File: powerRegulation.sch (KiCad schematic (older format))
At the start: 6 parts

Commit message: added additional regulator to power the ACS711 and potentially a micro at 3.3V
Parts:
- added C?: 4.7uF, symbol C
- added C?: 10uF, symbol C
- added L?: 4.7uH, symbol INDUCTOR_SMALL
- added R?: 976K, symbol R
- added R?: 562K, symbol R
- added U?: MCP1640T, SOT-23-6, symbol MCP1640T
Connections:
- net labels added: 3.3V
- wire segments 20 -> 45
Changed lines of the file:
@@
 Connection ~ 7200 2750
 Wire Wire Line
-	7200 3200 7200 2750
+	7200 2750 7200 3200
 Connection ~ 6800 2750
 Wire Wire Line
@@
 Connection ~ 6800 3950
 Wire Wire Line
-	7200 3600 7200 3950
+	7200 3950 7200 3600
 Connection ~ 5200 3950
 Wire Wire Line
@@
 	5800 3950 5800 4100
 Wire Wire Line
-	7200 3950 4850 3950
+	4850 3950 7200 3950
 Connection ~ 6800 3400
 Wire Wire Line
@@
 	6250 2900 6550 2900
 Wire Wire Line
-	6800 3450 6800 3350
+	6800 3350 6800 3450
 Text GLabel 8050 2750 2    60   Output ~ 0
 2.7V
@@
 Wire Wire Line
 	3900 2750 5350 2750
+$Comp
+L MCP1640T U?
+U 1 1 5522881E
+P 6550 4900
+F 0 "U?" H 6800 4650 40  0000 C CNN
+F 1 "MCP1640T" H 6800 5200 40  0000 C CNN
+F 2 "SOT-23-6" H 6550 4950 30  0000 C CIN
+F 3 "" H 6550 4900 60  0000 C CNN
+	1    6550 4900
+	1    0    0    -1
+$EndComp
+$Comp
+L INDUCTOR_SMALL L?
+U 1 1 55228894
+P 6000 4500
+F 0 "L?" H 6000 4600 50  0000 C CNN
+F 1 "4.7uH" H 6000 4450 50  0000 C CNN
+F 2 "" H 6000 4500 60  0000 C CNN
+F 3 "" H 6000 4500 60  0000 C CNN
+F 4 "Value" H 6000 4500 60  0001 C CNN "MPN"
+	1    6000 4500
+	1    0    0    -1
+$EndComp
+Wire Wire Line
+	6250 4500 6550 4500
+$Comp
+L GND #PWR?
+U 1 1 55228946
+P 6550 5450
+F 0 "#PWR?" H 6550 5200 60  0001 C CNN
+F 1 "GND" H 6550 5300 60  0000 C CNN
+F 2 "" H 6550 5450 60  0000 C CNN
+F 3 "" H 6550 5450 60  0000 C CNN
+	1    6550 5450
+	1    0    0    -1
+$EndComp
+Wire Wire Line
+	6550 5200 6550 5450
+Text GLabel 5250 4750 0    60   Input ~ 0
+2.7V
+Wire Wire Line
+	5250 4750 6100 4750
+Wire Wire Line
+	6100 4900 5950 4900
+Wire Wire Line
+	5950 4900 5950 4750
+Connection ~ 5950 4750
+$Comp
+L C C?
+U 1 1 55228B01
+P 5750 5150
+F 0 "C?" H 5800 5250 50  0000 L CNN
+F 1 "4.7uF" H 5800 5050 50  0000 L CNN
+F 2 "" H 5788 5000 30  0000 C CNN
+F 3 "" H 5750 5150 60  0000 C CNN
+F 4 "Value" H 5750 5150 60  0001 C CNN "MPN"
+	1    5750 5150
+	1    0    0    -1
+$EndComp
+Wire Wire Line
+	5750 4950 5750 4750
+Connection ~ 5750 4750
+Wire Wire Line
+	5750 5350 5750 5400
+Wire Wire Line
+	5750 5400 6550 5400
+Connection ~ 6550 5400
+Wire Wire Line
+	5750 4500 5550 4500
+Wire Wire Line
+	5550 4500 5550 4750
+Connection ~ 5550 4750
+$Comp
+L R R?
+U 1 1 55228C70
+P 7700 5050
+F 0 "R?" V 7780 5050 50  0000 C CNN
+F 1 "976K" V 7707 5051 50  0000 C CNN
+F 2 "" V 7630 5050 30  0000 C CNN
+F 3 "" H 7700 5050 30  0000 C CNN
+	1    7700 5050
+	1    0    0    -1
+$EndComp
+$Comp
+L R R?
+U 1 1 55228CAB
+P 7700 5650
+F 0 "R?" V 7780 5650 50  0000 C CNN
+F 1 "562K" V 7707 5651 50  0000 C CNN
+F 2 "" V 7630 5650 30  0000 C CNN
+F 3 "" H 7700 5650 30  0000 C CNN
+	1    7700 5650
+	1    0    0    -1
+$EndComp
+Text GLabel 8100 4750 2    60   Input ~ 0
+3.3V
+Wire Wire Line
+	7000 4750 8100 4750
+Wire Wire Line
+	7700 4800 7700 4750
+Connection ~ 7700 4750
+Wire Wire Line
+	7700 5300 7700 5400
+Wire Wire Line
+	7000 4900 7400 4900
+Wire Wire Line
+	7400 4900 7400 5350
+Wire Wire Line
+	7400 5350 7700 5350
+Connection ~ 7700 5350
+Wire Wire Line
+	7700 5900 7700 6000
+Wire Wire Line
+	7700 6000 7050 6000
+Wire Wire Line
+	7050 6000 7050 5300
+Wire Wire Line
+	7050 5300 6550 5300
+Connection ~ 6550 5300
+$Comp
+L C C?
+U 1 1 5522902B
+P 7950 5300
+F 0 "C?" H 8000 5400 50  0000 L CNN
+F 1 "10uF" H 8000 5200 50  0000 L CNN
+F 2 "" H 7988 5150 30  0000 C CNN
+F 3 "" H 7950 5300 60  0000 C CNN
+	1    7950 5300
+	1    0    0    -1
+$EndComp
+Wire Wire Line
+	7950 5100 7950 4750
+Connection ~ 7950 4750
+Wire Wire Line
+	7950 5500 7950 6050
+Wire Wire Line
+	7950 6050 6900 6050
+Wire Wire Line
+	6900 6050 6900 5350
+Wire Wire Line
+	6900 5350 6550 5350
+Connection ~ 6550 5350
 $EndSCHEMATC

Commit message: updated power regulation circuit with a different component so that the pin numbers now show
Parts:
- removed U?: LM2931D-R, symbol LM2931D-R
- added U?: LM2931, SO-8, symbol LM2931
- C?: value C -> 0.1uF
- C?: value C -> 100uF
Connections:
- wire segments 45 -> 65
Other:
- moved on the sheet: C?
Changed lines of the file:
@@
 L C C?
 U 1 1 5521C44E
-P 4850 3650
-F 0 "C?" H 4900 3750 50  0000 L CNN
-F 1 "C" H 4900 3550 50  0000 L CNN
-F 2 "" H 4888 3500 30  0000 C CNN
-F 3 "" H 4850 3650 60  0000 C CNN
-	1    4850 3650
+P 4850 3300
+F 0 "C?" H 4900 3400 50  0000 L CNN
+F 1 "0.1uF" H 4900 3200 50  0000 L CNN
+F 2 "" H 4888 3150 30  0000 C CNN
+F 3 "" H 4850 3300 60  0000 C CNN
+	1    4850 3300
 	-1   0    0    -1
 $EndComp
@@
 L C C?
 U 1 1 5521C455
-P 7200 3400
-F 0 "C?" H 7250 3500 50  0000 L CNN
-F 1 "C" H 7250 3300 50  0000 L CNN
-F 2 "" H 7238 3250 30  0000 C CNN
-F 3 "" H 7200 3400 60  0000 C CNN
-	1    7200 3400
-	-1   0    0    -1
-$EndComp
-$Comp
-L LM2931D-R U?
-U 1 1 5521C45C
-P 5800 3150
-F 0 "U?" H 6100 3100 60  0000 C CNN
-F 1 "LM2931D-R" H 5800 3650 60  0000 C CNN
-F 2 "" H 5650 3350 60  0000 C CNN
-F 3 "" H 5650 3350 60  0000 C CNN
-	1    5800 3150
-	1    0    0    -1
+P 7200 3300
+F 0 "C?" H 7250 3400 50  0000 L CNN
+F 1 "100uF" H 7250 3200 50  0000 L CNN
+F 2 "" H 7238 3150 30  0000 C CNN
+F 3 "" H 7200 3300 60  0000 C CNN
+	1    7200 3300
+	-1   0    0    -1
 $EndComp
 $Comp
@@
 	-1   0    0    -1
 $EndComp
-Connection ~ 7200 2750
-Wire Wire Line
-	7200 2750 7200 3200
-Connection ~ 6800 2750
-Wire Wire Line
-	6800 2850 6800 2750
-Connection ~ 6800 3950
-Wire Wire Line
-	7200 3950 7200 3600
-Connection ~ 5200 3950
-Wire Wire Line
-	5200 3550 5200 3950
-Wire Wire Line
-	5200 2900 5200 3050
-Wire Wire Line
-	5350 2900 5200 2900
-Connection ~ 4850 2750
-Wire Wire Line
-	4850 3450 4850 2750
-Connection ~ 5650 3950
-Wire Wire Line
-	4850 3950 4850 3850
-Connection ~ 5750 3950
-Wire Wire Line
-	5650 3950 5650 3200
-Connection ~ 5800 3950
-Wire Wire Line
-	5750 3950 5750 3200
-Connection ~ 5950 3950
-Wire Wire Line
-	5950 3200 5950 3950
-Connection ~ 5850 3950
-Wire Wire Line
-	5850 3200 5850 3950
-Wire Wire Line
-	5800 3950 5800 4100
-Wire Wire Line
-	4850 3950 7200 3950
-Connection ~ 6800 3400
-Wire Wire Line
-	6550 3400 6800 3400
-Wire Wire Line
-	6550 2900 6550 3400
-Wire Wire Line
-	6250 2900 6550 2900
-Wire Wire Line
-	6800 3350 6800 3450
 Text GLabel 8050 2750 2    60   Output ~ 0
 2.7V
-Wire Wire Line
-	6250 2750 8050 2750
 Text HLabel 3900 2750 0    60   Input ~ 0
 Vin
-Wire Wire Line
-	3900 2750 5350 2750
 $Comp
 L MCP1640T U?
@@
 	1    0    0    -1
 $EndComp
-Wire Wire Line
-	6250 4500 6550 4500
 $Comp
 L GND #PWR?
@@
 	1    0    0    -1
 $EndComp
-Wire Wire Line
-	6550 5200 6550 5450
 Text GLabel 5250 4750 0    60   Input ~ 0
 2.7V
-Wire Wire Line
-	5250 4750 6100 4750
-Wire Wire Line
-	6100 4900 5950 4900
-Wire Wire Line
-	5950 4900 5950 4750
-Connection ~ 5950 4750
 $Comp
 L C C?
@@
 	1    0    0    -1
 $EndComp
-Wire Wire Line
-	5750 4950 5750 4750
-Connection ~ 5750 4750
-Wire Wire Line
-	5750 5350 5750 5400
-Wire Wire Line
-	5750 5400 6550 5400
-Connection ~ 6550 5400
-Wire Wire Line
-	5750 4500 5550 4500
-Wire Wire Line
-	5550 4500 5550 4750
-Connection ~ 5550 4750
 $Comp
 L R R?
@@
 Text GLabel 8100 4750 2    60   Input ~ 0
 3.3V
-Wire Wire Line
-	7000 4750 8100 4750
-Wire Wire Line
-	7700 4800 7700 4750
-Connection ~ 7700 4750
-Wire Wire Line
-	7700 5300 7700 5400
-Wire Wire Line
-	7000 4900 7400 4900
-Wire Wire Line
-	7400 4900 7400 5350
-Wire Wire Line
-	7400 5350 7700 5350
-Connection ~ 7700 5350
-Wire Wire Line
-	7700 5900 7700 6000
-Wire Wire Line
-	7700 6000 7050 6000
-Wire Wire Line
-	7050 6000 7050 5300
-Wire Wire Line
-	7050 5300 6550 5300
-Connection ~ 6550 5300
 $Comp
 L C C?
@@
 	1    0    0    -1
 $EndComp
+Connection ~ 7200 2750
+Wire Wire Line
+	7200 2750 7200 3100
+Connection ~ 6800 2750
+Wire Wire Line
+	6800 2850 6800 2750
+Connection ~ 6800 3950
+Wire Wire Line
+	7200 3950 7200 3500
+Connection ~ 5200 3950
+Wire Wire Line
+	5200 3550 5200 3950
+Wire Wire Line
+	5200 2850 5200 3050
+Connection ~ 4850 2750
+Wire Wire Line
+	4850 3100 4850 2750
+Connection ~ 5650 3950
+Wire Wire Line
+	4850 3950 4850 3500
+Connection ~ 5750 3950
+Wire Wire Line
+	5650 3950 5650 3200
+Connection ~ 5800 3950
+Wire Wire Line
+	5750 3950 5750 3200
+Connection ~ 5950 3950
+Wire Wire Line
+	5950 3200 5950 3950
+Connection ~ 5850 3950
+Wire Wire Line
+	5850 3200 5850 3950
+Wire Wire Line
+	5800 3950 5800 4100
+Wire Wire Line
+	4850 3950 5200 3950
+Wire Wire Line
+	5200 3950 5650 3950
+Wire Wire Line
+	5650 3950 5750 3950
+Wire Wire Line
+	5750 3950 5800 3950
+Wire Wire Line
+	5800 3950 5850 3950
+Wire Wire Line
+	5850 3950 5950 3950
+Wire Wire Line
+	5950 3950 6800 3950
+Wire Wire Line
+	6800 3950 7200 3950
+Connection ~ 6800 3400
+Wire Wire Line
+	6550 3400 6800 3400
+Wire Wire Line
+	6550 2850 6550 3400
+Wire Wire Line
+	6800 3350 6800 3400
+Wire Wire Line
+	6800 3400 6800 3450
+Wire Wire Line
+	6200 2750 6800 2750
+Wire Wire Line
+	6800 2750 7200 2750
+Wire Wire Line
+	7200 2750 8050 2750
+Wire Wire Line
+	3900 2750 4850 2750
+Wire Wire Line
+	4850 2750 5400 2750
+Wire Wire Line
+	6250 4500 6550 4500
+Wire Wire Line
+	6550 5200 6550 5300
+Wire Wire Line
+	6550 5300 6550 5350
+Wire Wire Line
+	6550 5350 6550 5400
+Wire Wire Line
+	6550 5400 6550 5450
+Wire Wire Line
+	5250 4750 5550 4750
+Wire Wire Line
+	5550 4750 5750 4750
+Wire Wire Line
+	5750 4750 5950 4750
+Wire Wire Line
+	5950 4750 6100 4750
+Wire Wire Line
+	6100 4900 5950 4900
+Wire Wire Line
+	5950 4900 5950 4750
+Connection ~ 5950 4750
+Wire Wire Line
+	5750 4950 5750 4750
+Connection ~ 5750 4750
+Wire Wire Line
+	5750 5350 5750 5400
+Wire Wire Line
+	5750 5400 6550 5400
+Connection ~ 6550 5400
+Wire Wire Line
+	5750 4500 5550 4500
+Wire Wire Line
+	5550 4500 5550 4750
+Connection ~ 5550 4750
+Wire Wire Line
+	7000 4750 7700 4750
+Wire Wire Line
+	7700 4750 7950 4750
+Wire Wire Line
+	7950 4750 8100 4750
+Wire Wire Line
+	7700 4800 7700 4750
+Connection ~ 7700 4750
+Wire Wire Line
+	7700 5300 7700 5350
+Wire Wire Line
+	7700 5350 7700 5400
+Wire Wire Line
+	7000 4900 7400 4900
+Wire Wire Line
+	7400 4900 7400 5350
+Wire Wire Line
+	7400 5350 7700 5350
+Connection ~ 7700 5350
+Wire Wire Line
+	7700 5900 7700 6000
+Wire Wire Line
+	7700 6000 7050 6000
+Wire Wire Line
+	7050 6000 7050 5300
+Wire Wire Line
+	7050 5300 6550 5300
+Connection ~ 6550 5300
 Wire Wire Line
 	7950 5100 7950 4750
@@
 	6900 5350 6550 5350
 Connection ~ 6550 5350
+$Comp
+L LM2931 U?
+U 1 1 55220147
+P 5800 2800
+F 0 "U?" H 5600 3000 40  0000 C CNN
+F 1 "LM2931" H 5800 3000 40  0000 L CNN
+F 2 "SO-8" H 5800 2900 30  0000 C CIN
+F 3 "" H 5800 2700 60  0000 C CNN
+	1    5800 2800
+	1    0    0    -1
+$EndComp
+Wire Wire Line
+	5200 2850 5400 2850
+Wire Wire Line
+	6550 2850 6200 2850
 $EndSCHEMATC

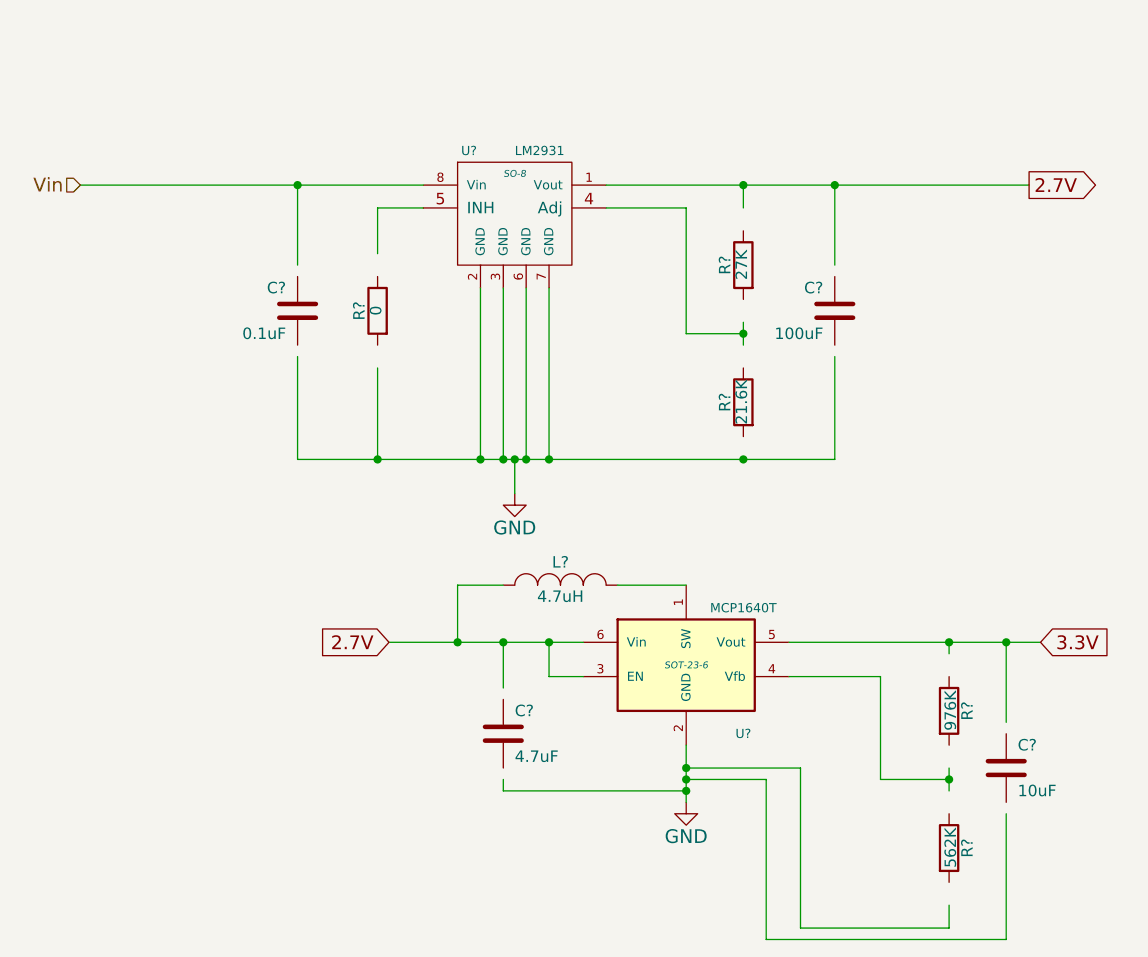
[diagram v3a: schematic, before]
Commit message: updated with association labels
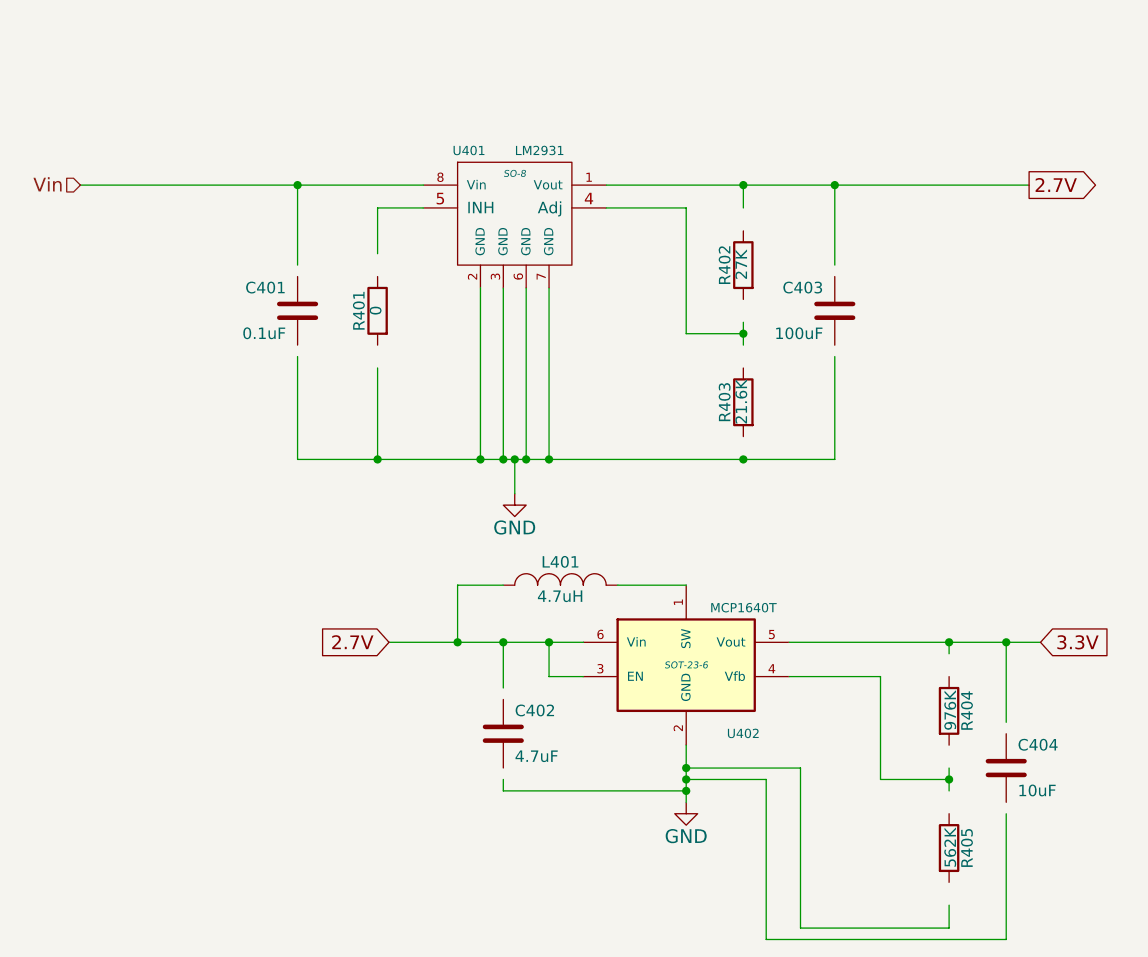
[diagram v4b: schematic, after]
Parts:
- gave numbers to parts that had none: 12
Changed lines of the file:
@@
 $EndDescr
 $Comp
-L GND #PWR?
+L GND #PWR401
 U 1 1 5521C448
 P 5800 4100
-F 0 "#PWR?" H 5800 3850 60  0001 C CNN
+F 0 "#PWR401" H 5800 3850 60  0001 C CNN
 F 1 "GND" H 5800 3950 60  0000 C CNN
 F 2 "" H 5800 4100 60  0000 C CNN
@@
 $EndComp
 $Comp
-L C C?
+L C C401
 U 1 1 5521C44E
 P 4850 3300
-F 0 "C?" H 4900 3400 50  0000 L CNN
+F 0 "C401" H 4900 3400 50  0000 L CNN
 F 1 "0.1uF" H 4900 3200 50  0000 L CNN
 F 2 "" H 4888 3150 30  0000 C CNN
@@
 $EndComp
 $Comp
-L C C?
+L C C403
 U 1 1 5521C455
 P 7200 3300
-F 0 "C?" H 7250 3400 50  0000 L CNN
+F 0 "C403" H 7250 3400 50  0000 L CNN
 F 1 "100uF" H 7250 3200 50  0000 L CNN
 F 2 "" H 7238 3150 30  0000 C CNN
@@
 $EndComp
 $Comp
-L R R?
+L R R402
 U 1 1 5521C463
 P 6800 3100
-F 0 "R?" V 6880 3100 50  0000 C CNN
+F 0 "R402" V 6880 3100 50  0000 C CNN
 F 1 "27K" V 6807 3101 50  0000 C CNN
 F 2 "" V 6730 3100 30  0000 C CNN
@@
 $EndComp
 $Comp
-L R R?
+L R R403
 U 1 1 5521C46A
 P 6800 3700
-F 0 "R?" V 6880 3700 50  0000 C CNN
+F 0 "R403" V 6880 3700 50  0000 C CNN
 F 1 "21.6K" V 6807 3701 50  0000 C CNN
 F 2 "" V 6730 3700 30  0000 C CNN
@@
 $EndComp
 $Comp
-L R R?
+L R R401
 U 1 1 5521C471
 P 5200 3300
-F 0 "R?" V 5280 3300 50  0000 C CNN
+F 0 "R401" V 5280 3300 50  0000 C CNN
 F 1 "0" V 5207 3301 50  0000 C CNN
 F 2 "" V 5130 3300 30  0000 C CNN
@@
 Vin
 $Comp
-L MCP1640T U?
+L MCP1640T U402
 U 1 1 5522881E
 P 6550 4900
-F 0 "U?" H 6800 4650 40  0000 C CNN
+F 0 "U402" H 6800 4650 40  0000 C CNN
 F 1 "MCP1640T" H 6800 5200 40  0000 C CNN
 F 2 "SOT-23-6" H 6550 4950 30  0000 C CIN
@@
 $EndComp
 $Comp
-L INDUCTOR_SMALL L?
+L INDUCTOR_SMALL L401
 U 1 1 55228894
 P 6000 4500
-F 0 "L?" H 6000 4600 50  0000 C CNN
+F 0 "L401" H 6000 4600 50  0000 C CNN
 F 1 "4.7uH" H 6000 4450 50  0000 C CNN
 F 2 "" H 6000 4500 60  0000 C CNN
@@
 $EndComp
 $Comp
-L GND #PWR?
+L GND #PWR402
 U 1 1 55228946
 P 6550 5450
-F 0 "#PWR?" H 6550 5200 60  0001 C CNN
+F 0 "#PWR402" H 6550 5200 60  0001 C CNN
 F 1 "GND" H 6550 5300 60  0000 C CNN
 F 2 "" H 6550 5450 60  0000 C CNN
@@
 2.7V
 $Comp
-L C C?
+L C C402
 U 1 1 55228B01
 P 5750 5150
-F 0 "C?" H 5800 5250 50  0000 L CNN
+F 0 "C402" H 5800 5250 50  0000 L CNN
 F 1 "4.7uF" H 5800 5050 50  0000 L CNN
 F 2 "" H 5788 5000 30  0000 C CNN
@@
 $EndComp
 $Comp
-L R R?
+L R R404
 U 1 1 55228C70
 P 7700 5050
-F 0 "R?" V 7780 5050 50  0000 C CNN
+F 0 "R404" V 7780 5050 50  0000 C CNN
 F 1 "976K" V 7707 5051 50  0000 C CNN
 F 2 "" V 7630 5050 30  0000 C CNN
@@
 $EndComp
 $Comp
-L R R?
+L R R405
 U 1 1 55228CAB
 P 7700 5650
-F 0 "R?" V 7780 5650 50  0000 C CNN
+F 0 "R405" V 7780 5650 50  0000 C CNN
 F 1 "562K" V 7707 5651 50  0000 C CNN
 F 2 "" V 7630 5650 30  0000 C CNN
@@
 3.3V
 $Comp
-L C C?
+L C C404
 U 1 1 5522902B
 P 7950 5300
-F 0 "C?" H 8000 5400 50  0000 L CNN
+F 0 "C404" H 8000 5400 50  0000 L CNN
 F 1 "10uF" H 8000 5200 50  0000 L CNN
 F 2 "" H 7988 5150 30  0000 C CNN
@@
 Connection ~ 6550 5350
 $Comp
-L LM2931 U?
+L LM2931 U401
 U 1 1 55220147
 P 5800 2800
-F 0 "U?" H 5600 3000 40  0000 C CNN
+F 0 "U401" H 5600 3000 40  0000 C CNN
 F 1 "LM2931" H 5800 3000 40  0000 L CNN
 F 2 "SO-8" H 5800 2900 30  0000 C CIN
